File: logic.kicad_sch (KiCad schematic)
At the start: 20 parts, among them U1 ESP32-C3-MINI-1, U10 LIS3DH, U5 SPL06-001, U7 LTR-303ALS-01

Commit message: logic: connect pressure sensor via I2C
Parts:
- added R12: 100k, Resistor_SMD:R_0402_1005Metric, symbol Device:R_Small
- added R12 (x2): 10k, Resistor_SMD:R_0402_1005Metric, symbol Device:R_Small
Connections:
- net +3V3: now also U5.2 (CSB), R12.1, R12.1
- net GND: now also R12.2
- net SCL: now also U5.4 (SCK)
- net SDA: now also U5.3 (SDA)
- net at U7.5 (INT): now also U1.19 (IO5), R12.2
- net at U10.11 (INT1): now also U1.20 (IO6)
- net at U10.9 (INT2): now also U1.21 (IO7)
- net at R12.2, U1.23 (IO9): now also U6.3 (CLK); no longer U5.2 (CSB)
- net at R12.2, U1.16 (IO10): now also R12.1
- net at U5.5 (SDO): now also U1.22 (IO8), R12.2; no longer U1.20 (IO6)
- no-connect marks 6 -> 3
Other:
- moved on the sheet: C5, R12, U1, U10, U5, U6, U7

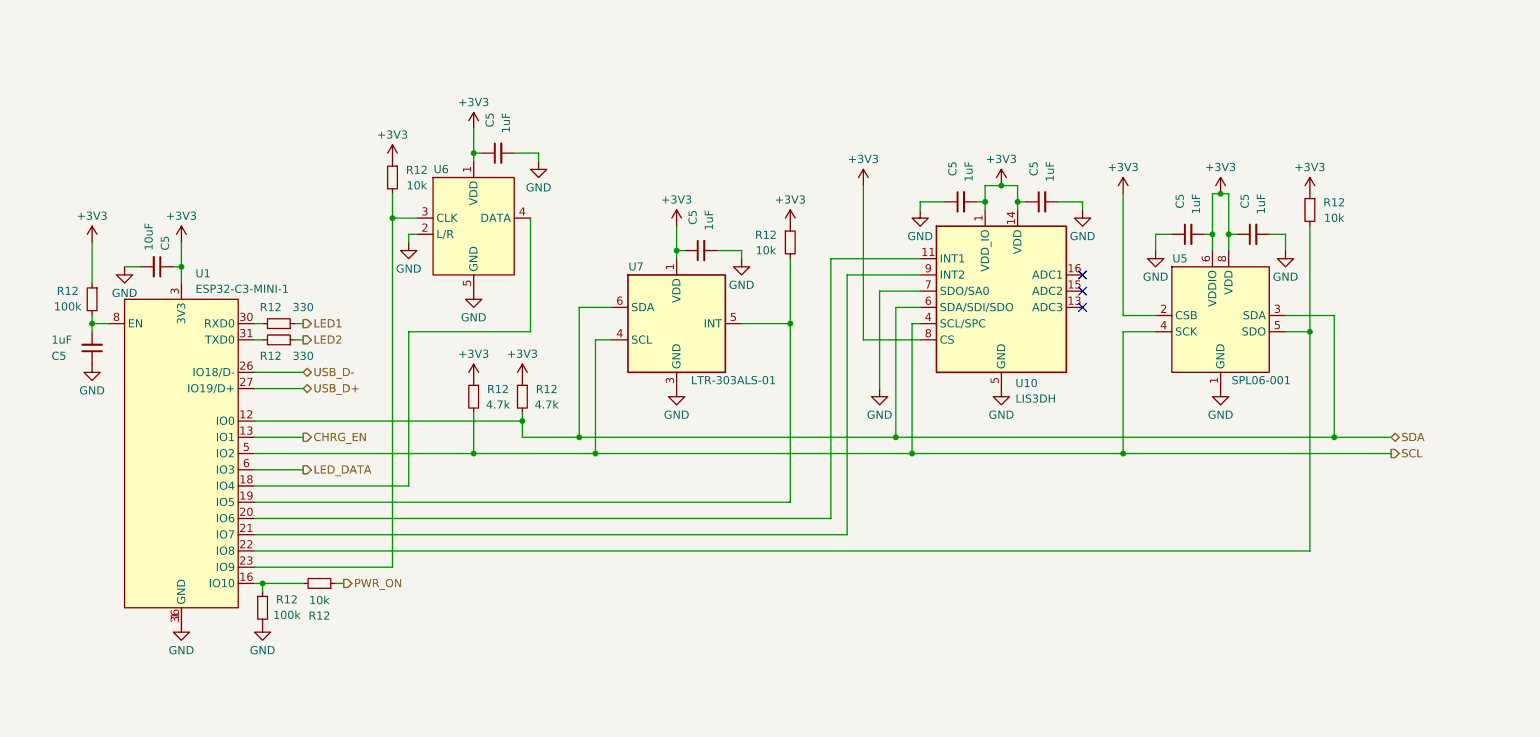
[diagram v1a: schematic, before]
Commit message: Relayout board to fit constraints of Micro USB Blinkekatzen
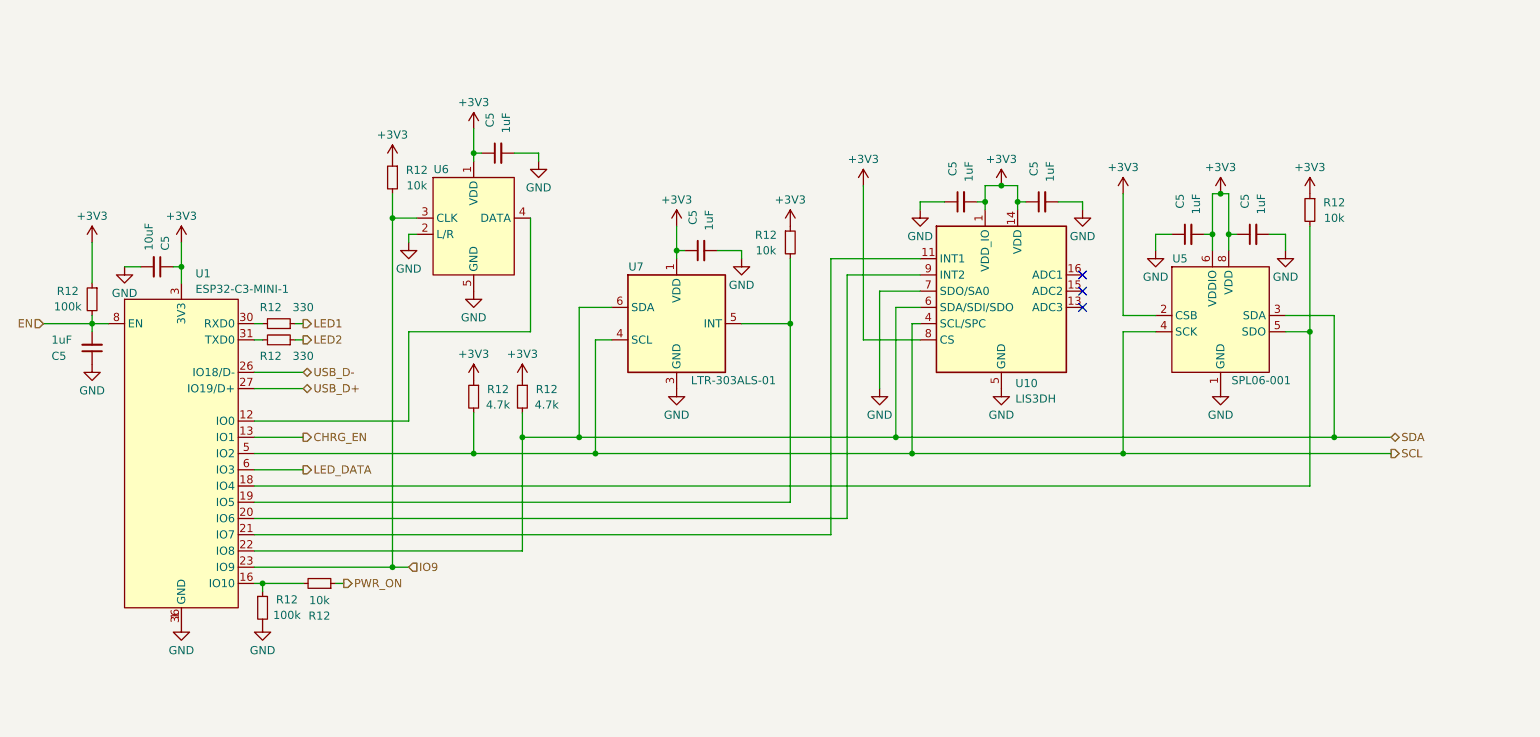
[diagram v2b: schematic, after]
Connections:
- net SDA: now also U1.22 (IO8); no longer U1.12 (IO0)
- net EN: now reaches C5.2, R12.2, U1.8 (EN)
- net at U10.11 (INT1): now also U1.21 (IO7); no longer U1.20 (IO6)
- net at U10.9 (INT2): now also U1.20 (IO6); no longer U1.21 (IO7)
- net IO9: now reaches R12.2, U1.23 (IO9), U6.3 (CLK)
- net at U6.4 (DATA): now also U1.12 (IO0); no longer U1.18 (IO4)
- net at R12.2, U5.5 (SDO): now also U1.18 (IO4); no longer U1.22 (IO8)
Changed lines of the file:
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@@
 (kicad_sch (version 20230121) (generator eeschema)
   (paper "A4")
+  (junction (at 95.25 119.38) (diameter 0) (color 0 0 0 0)
+  )
   (junction (at 224.79 60.96) (diameter 0) (color 0 0 0 0)
   )
+  (junction (at 115.57 99.06) (diameter 0) (color 0 0 0 0)
+  )
   (junction (at 139.7 69.85) (diameter 0) (color 0 0 0 0)
   )
@@
   )
   (junction (at 187.96 62.23) (diameter 0) (color 0 0 0 0)
-  )
-  (junction (at 115.57 96.52) (diameter 0) (color 0 0 0 0)
   )
   (junction (at 190.5 59.69) (diameter 0) (color 0 0 0 0)
@@
     (stroke (width 0) (type default))
   )
+  (wire (pts (xy 40.64 81.28) (xy 48.26 81.28))
+    (stroke (width 0) (type default))
+  )
   (wire (pts (xy 176.53 101.6) (xy 209.55 101.6))
     (stroke (width 0) (type default))
   )
-  (wire (pts (xy 97.79 82.55) (xy 97.79 106.68))
+  (wire (pts (xy 97.79 82.55) (xy 97.79 96.52))
     (stroke (width 0) (type default))
   )
@@
     (stroke (width 0) (type default))
   )
-  (wire (pts (xy 73.66 111.76) (xy 163.83 111.76))
-    (stroke (width 0) (type default))
-  )
   (wire (pts (xy 238.76 82.55) (xy 234.95 82.55))
     (stroke (width 0) (type default))
@@
     (stroke (width 0) (type default))
   )
+  (wire (pts (xy 166.37 73.66) (xy 166.37 111.76))
+    (stroke (width 0) (type default))
+  )
   (wire (pts (xy 224.79 60.96) (xy 223.52 60.96))
     (stroke (width 0) (type default))
   )
-  (wire (pts (xy 73.66 96.52) (xy 115.57 96.52))
+  (wire (pts (xy 73.66 96.52) (xy 97.79 96.52))
     (stroke (width 0) (type default))
   )
@@
     (stroke (width 0) (type default))
   )
+  (wire (pts (xy 73.66 106.68) (xy 238.76 106.68))
+    (stroke (width 0) (type default))
+  )
   (wire (pts (xy 157.48 109.22) (xy 73.66 109.22))
     (stroke (width 0) (type default))
@@
     (stroke (width 0) (type default))
   )
-  (wire (pts (xy 115.57 96.52) (xy 115.57 99.06))
+  (wire (pts (xy 115.57 95.25) (xy 115.57 99.06))
     (stroke (width 0) (type default))
   )
@@
     (stroke (width 0) (type default))
   )
-  (wire (pts (xy 238.76 82.55) (xy 238.76 116.84))
+  (wire (pts (xy 238.76 82.55) (xy 238.76 106.68))
     (stroke (width 0) (type default))
   )
@@
     (stroke (width 0) (type default))
   )
+  (wire (pts (xy 73.66 111.76) (xy 166.37 111.76))
+    (stroke (width 0) (type default))
+  )
+  (wire (pts (xy 115.57 99.06) (xy 115.57 116.84))
+    (stroke (width 0) (type default))
+  )
   (wire (pts (xy 80.01 81.28) (xy 81.28 81.28))
     (stroke (width 0) (type default))
@@
     (stroke (width 0) (type default))
   )
+  (wire (pts (xy 73.66 116.84) (xy 115.57 116.84))
+    (stroke (width 0) (type default))
+  )
   (wire (pts (xy 140.97 69.85) (xy 139.7 69.85))
     (stroke (width 0) (type default))
   )
-  (wire (pts (xy 163.83 111.76) (xy 163.83 71.12))
-    (stroke (width 0) (type default))
-  )
-  (wire (pts (xy 166.37 114.3) (xy 73.66 114.3))
+  (wire (pts (xy 163.83 71.12) (xy 163.83 114.3))
+    (stroke (width 0) (type default))
+  )
+  (wire (pts (xy 95.25 119.38) (xy 97.79 119.38))
     (stroke (width 0) (type default))
   )
@@
     (stroke (width 0) (type default))
   )
-  (wire (pts (xy 166.37 73.66) (xy 166.37 114.3))
-    (stroke (width 0) (type default))
-  )
   (wire (pts (xy 107.95 50.8) (xy 107.95 54.61))
     (stroke (width 0) (type default))
@@
     (stroke (width 0) (type default))
   )
-  (wire (pts (xy 115.57 95.25) (xy 115.57 96.52))
-    (stroke (width 0) (type default))
-  )
   (wire (pts (xy 73.66 81.28) (xy 74.93 81.28))
     (stroke (width 0) (type default))
@@
     (stroke (width 0) (type default))
   )
+  (wire (pts (xy 73.66 114.3) (xy 163.83 114.3))
+    (stroke (width 0) (type default))
+  )
   (wire (pts (xy 80.01 83.82) (xy 81.28 83.82))
     (stroke (width 0) (type default))
@@
     (stroke (width 0) (type default))
   )
-  (wire (pts (xy 73.66 106.68) (xy 97.79 106.68))
-    (stroke (width 0) (type default))
-  )
   (wire (pts (xy 223.52 60.96) (xy 223.52 67.31))
     (stroke (width 0) (type default))
@@
     (stroke (width 0) (type default))
   )
-  (wire (pts (xy 238.76 116.84) (xy 73.66 116.84))
-    (stroke (width 0) (type default))
-  )
   (wire (pts (xy 116.84 64.77) (xy 116.84 82.55))
     (stroke (width 0) (type default))
@@
     (effects (font (size 1.27 1.27)) (justify left))
   )
+  (hierarchical_label "IO9" (shape input) (at 97.79 119.38 0) (fields_autoplaced)
+    (effects (font (size 1.27 1.27)) (justify left))
+  )
   (hierarchical_label "PWR_ON" (shape output) (at 87.63 121.92 0) (fields_autoplaced)
     (effects (font (size 1.27 1.27)) (justify left))
@@
     (effects (font (size 1.27 1.27)) (justify left))
   )
+  (hierarchical_label "EN" (shape input) (at 40.64 81.28 180) (fields_autoplaced)
+    (effects (font (size 1.27 1.27)) (justify right))
+  )
   (hierarchical_label "LED_DATA" (shape output) (at 81.28 104.14 0) (fields_autoplaced)

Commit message: logic: update LCSC partnumbers
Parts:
- U1: LCSC C2838502 -> C2934569
- U6: LCSC C503097 -> C2688664
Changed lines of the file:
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@@
       (effects (font (size 1.27 1.27)) hide)
     )
-    (property "LCSC" "C2838502" (at 62.23 102.87 0)
+    (property "LCSC" "C2934569" (at 62.23 102.87 0)
       (effects (font (size 1.27 1.27)) hide)
     )
@@
       (effects (font (size 1.27 1.27)) hide)
     )
-    (property "LCSC" "C503097" (at 107.95 66.04 0)
-      (effects (font (size 1.27 1.27)) hide)
-    )
+    (property "LCSC" "C2688664" (at 107.95 66.04 0)
+      (effects (font (size 1.27 1.27)) hide)
+    )
